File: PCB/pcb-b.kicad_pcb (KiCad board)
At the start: 2 copper layers, 109.8 x 43.6 mm, 86 parts, among them K1 HK19F-DCxxV-SHC, Q1 BC817, Q10 BC817, Q11 TPCA8120,L1Q, Q12 BC817, Q13 TPCA8120,L1Q, Q14 BC817, Q15 BC817, Q17 BC327, Q18 BC327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

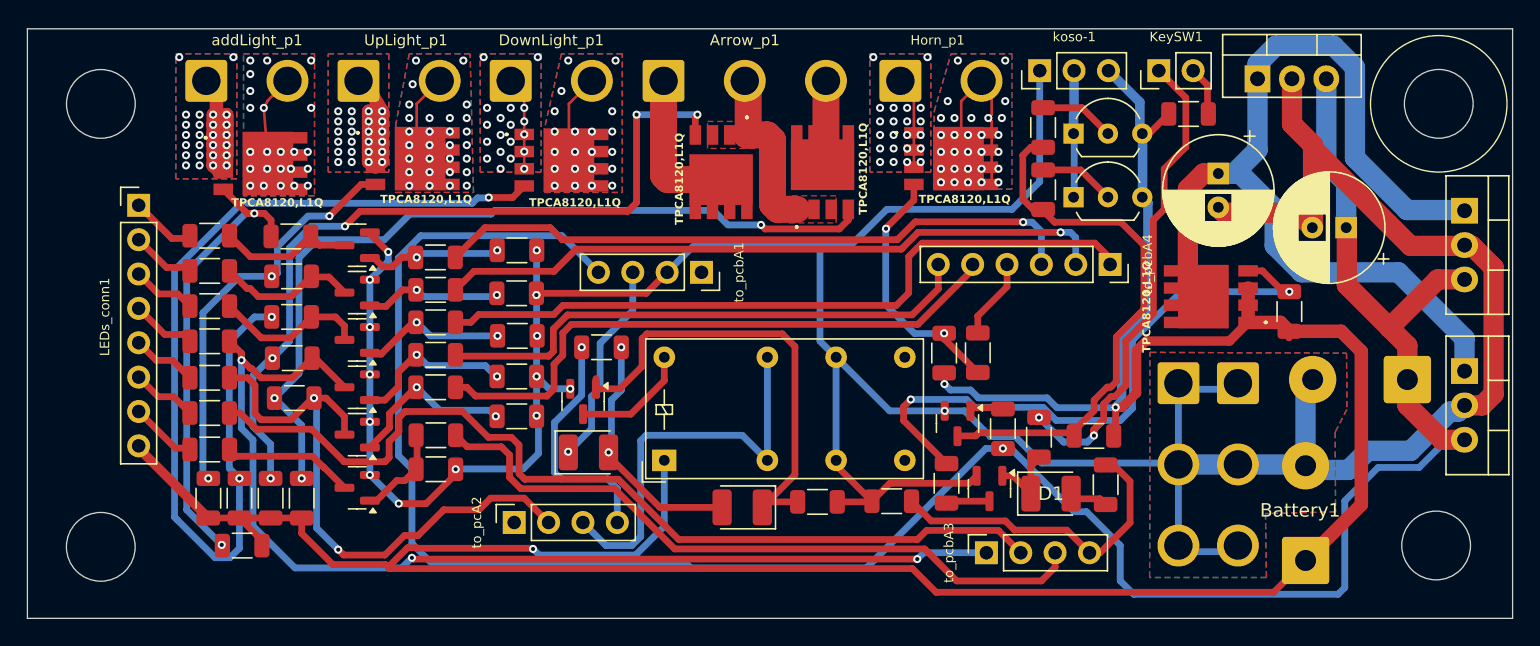
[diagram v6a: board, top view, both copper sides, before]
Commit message: No USB support and PCB-B size reducing
Implementing USB power support using 7805 was a stupid idea: too much wasted electic current in Joule effect. So, I moved just
one 7805 in the PCB-A, because the its used power is very low. It allowed me to optimize the PCB-B used space and reduce its
whole size ;-)
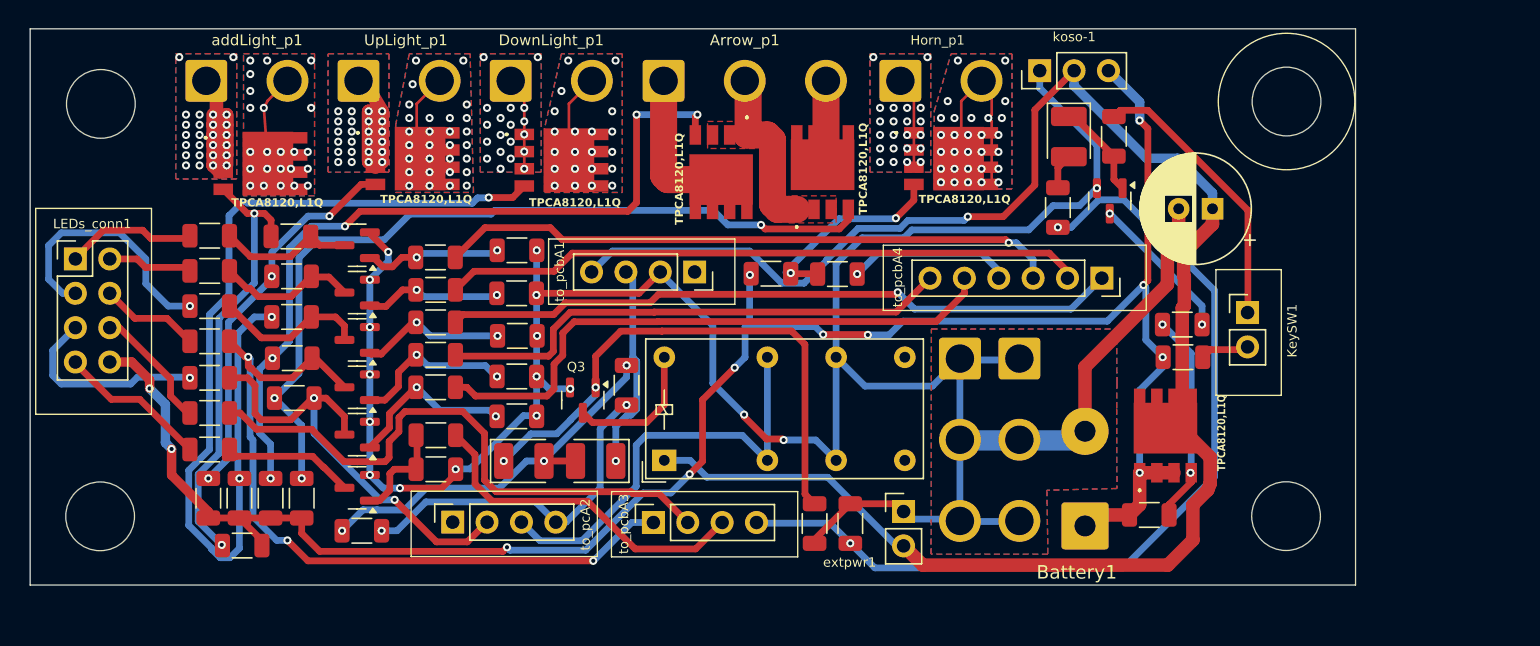
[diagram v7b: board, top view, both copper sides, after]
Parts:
- removed C1: C_Polarized_Small, Capacitor_THT:CP_Radial_D8.0mm_P2.50mm
- removed Q10, Q12: BC817, Package_TO_SOT_SMD:SOT-23
- removed Q17, Q18: BC327, Package_TO_SOT_THT:TO-92L_Inline_Wide
- removed RA23, RA30: 100K, Resistor_SMD:R_1206_3216Metric
- removed RA31, RA33: 3K, Resistor_SMD:R_1206_3216Metric
- removed U1, U2, U3: L7805, Package_TO_SOT_THT:TO-220-3_Vertical
- removed USB-5V1: Conn_01x02, Connector_Wire:SolderWire-0.75sqmm_1x02_P7mm_D1.25mm_OD3.5mm
- added Q3: BC817, Package_TO_SOT_SMD:SOT-23, F.Cu at (143.2, 97.7)
- added RA15: 10K, Resistor_SMD:R_1206_3216Metric, F.Cu at (126.9, 107.4)
- added extpwr1: Conn_01x02, Connector_PinHeader_2.54mm:PinHeader_1x02_P2.54mm_Vertical, F.Cu at (166.9, 105.9)
- LEDs_conn1: footprint Connector_PinHeader_2.54mm:PinHeader_1x08_P2.54mm_Vertical -> Connector_PinHeader_2.54mm:PinHeader_2x04_P2.54mm_Vertical
- RA8: value 10K -> 100K
- moved D1 26.4 mm to (179.2, 78.2), turned to -90 degrees
- moved to_pcbA3 24.7 mm to (148.4, 106.7)
- moved Q9 23.0 mm to (182.2, 83.0)
- moved R4 22.9 mm to (182.5, 78.2)
- moved R3 21.0 mm to (187.5, 92.1), turned to 180 degrees
- moved R5 20.8 mm to (178.3, 83.5), turned to -90 degrees
- moved KeySW1 19.0 mm to (192.4, 91.2), turned to 0 degrees
- moved R2 18.3 mm to (185.1, 106.2), turned to 0 degrees
- moved R1 18.0 mm to (187.6, 94.5)
- moved Battery1 16.5 mm to (180.3, 107.0)
- moved GND-1 16.3 mm to (175.5, 94.6)
- moved GND-2 16.2 mm to (171.1, 94.6)
- moved RA8 15.6 mm to (160.4, 106.8), turned to -90 degrees
- moved RA42 14.1 mm to (157.1, 88.4), turned to 180 degrees
- moved RA7 11.9 mm to (162.0, 88.4), turned to 0 degrees
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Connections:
- C9 pad 1: Net-(Q13-D_1) -> tempPower
- D2 pad 1: i_powerOFF -> Net-(D2-K)
- D3 pad 1: Net-(D3-K) -> i_powerOFF
- K1 pad A1: +12V -> tempPower
- Q13 pad 5: Net-(Q13-D_1) -> tempPower
- Q13 pad 6: Net-(Q13-D_1) -> tempPower
- Q13 pad 7: Net-(Q13-D_1) -> tempPower
- Q13 pad 8: Net-(Q13-D_1) -> tempPower
- Q13 pad 9: Net-(Q13-D_1) -> tempPower
- RA8 pad 1: tempPower -> Net-(D2-K)
- RA8 pad 2: Net-(Q10-B) -> GND
- koso-1 pad 2: Net-(Q17-C) -> tempPower
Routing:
- net Net-(Q13-D_1): track 73.2 -> 0.00 mm
- net +12V: track 211.4 -> 148.0 mm, vias 3 -> 12
- net GND: track 261.0 -> 201.6 mm, vias 15 -> 17
- net o_keepAlive: track 24.0 -> 67.0 mm, vias 0 -> 2
- net Net-(Q10-C): track 40.6 -> 0.00 mm
- net Net-(D2-K): track 0.00 -> 40.4 mm, vias 0 -> 2
- net tempPower: track 173.7 -> 134.8 mm
- net Net-(D3-K): track 34.4 -> 0.00 mm
- net Net-(Q13-G): track 45.5 -> 15.6 mm
- net o_engineReady: track 51.2 -> 25.3 mm
- net c_neutral: track 68.9 -> 43.6 mm
- net c_leftArrow: track 80.0 -> 55.6 mm
- net Net-(KeySW1-Pin_1): track 37.2 -> 20.7 mm, vias 2 -> 0
- net Net-(LEDs_conn1-Pin_3): track 4.77 -> 19.1 mm, vias 0 -> 1
- net c_rightArrow: track 43.7 -> 32.9 mm
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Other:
- board size 109.8 x 43.6 mm -> 98 x 41.1 mm

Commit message: PCB size reduction
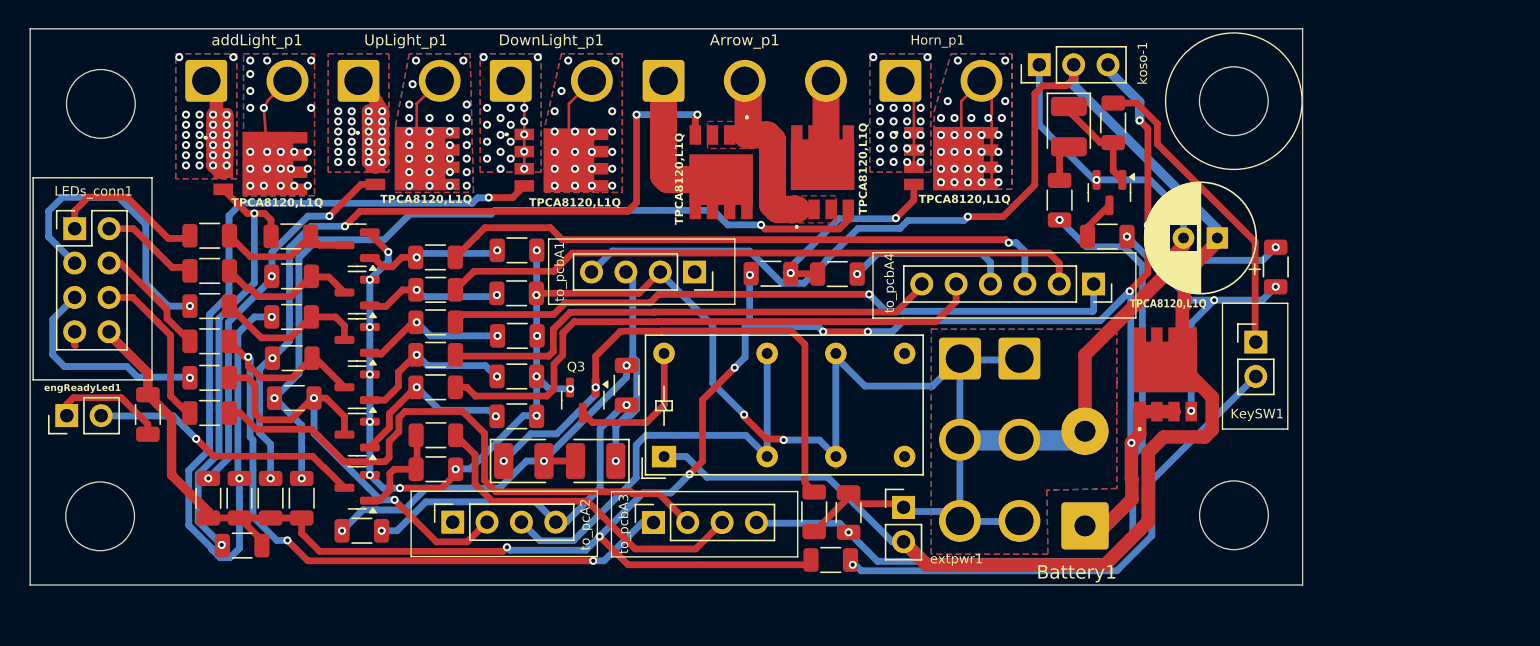
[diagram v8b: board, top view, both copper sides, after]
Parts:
- added engReadyLed1: Conn_01x02, Connector_PinHeader_2.54mm:PinHeader_1x02_P2.54mm_Vertical, F.Cu at (105.1, 98.8)
- RA9: value 0 -> 1K
- moved R1 30.0 mm to (161.6, 109.5)
- moved R2 20.6 mm to (194.4, 87.9), turned to -90 degrees
- moved R3 8.55 mm to (182.0, 85.6), turned to 0 degrees
- moved RA9 5.25 mm to (111.1, 98.8), turned to 90 degrees
- moved Q13 4.52 mm to (186.3, 95.8)
- moved KeySW1 2.27 mm to (193.0, 93.4)
- moved LEDs_conn1 2.24 mm to (105.7, 85.0)
- moved C9 2.19 mm to (190.1, 85.7)
- moved R4 1.00 mm to (182.4, 77.2)
- moved RA8 0.86 mm to (160.3, 106.0)
- moved R6 0.82 mm to (162.9, 106.0)
- moved to_pcbA4 0.75 mm to (181.0, 89.1)
- moved D1 0.74 mm to (179.2, 77.5)
- moved Q9 0.61 mm to (182.2, 82.4)
- moved R5 0.56 mm to (178.5, 82.9)
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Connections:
- LEDs_conn1 pad 7: Net-(LEDs_conn1-Pin_7) -> unconnected-(LEDs_conn1-Pin_7-Pad7)
- RA9 pad 1: Net-(Q21-C) -> Net-(engReadyLed1-Pin_1)
- RA9 pad 2: Net-(LEDs_conn1-Pin_7) -> +12V
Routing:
- net Net-(KeySW1-Pin_2): track 3.63 -> 38.6 mm, vias 0 -> 1
- net +12V: track 148.0 -> 177.5 mm
- net GND: track 201.6 -> 181.1 mm
- net Net-(LEDs_conn1-Pin_7): track 11.2 -> 0.00 mm
- net Net-(Q21-C): track 9.67 -> 20.2 mm, vias 0 -> 1
- net o_keepAlive: track 67.0 -> 57.7 mm
- net Net-(engReadyLed1-Pin_1): track 0.00 -> 8.58 mm
- net Net-(Q9-C): track 11.0 -> 2.99 mm, vias 2 -> 0
- net Net-(Q13-G): track 15.6 -> 22.2 mm, vias 2 -> 4
- net Net-(LEDs_conn1-Pin_6): track 9.28 -> 12.1 mm
- net Net-(LEDs_conn1-Pin_3): track 19.1 -> 21.4 mm
- net Net-(KeySW1-Pin_1): track 20.7 -> 23.0 mm
- net Net-(LEDs_conn1-Pin_1): track 9.71 -> 11.6 mm
- net Net-(LEDs_conn1-Pin_4): track 7.39 -> 8.75 mm
- net unconnected-(LEDs_conn1-Pin_7-Pad7): track 0.00 -> 1.04 mm
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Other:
- board size 98 x 41.1 mm -> 94.1 x 41.1 mm
